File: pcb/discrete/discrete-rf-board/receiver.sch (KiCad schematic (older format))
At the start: 4 parts

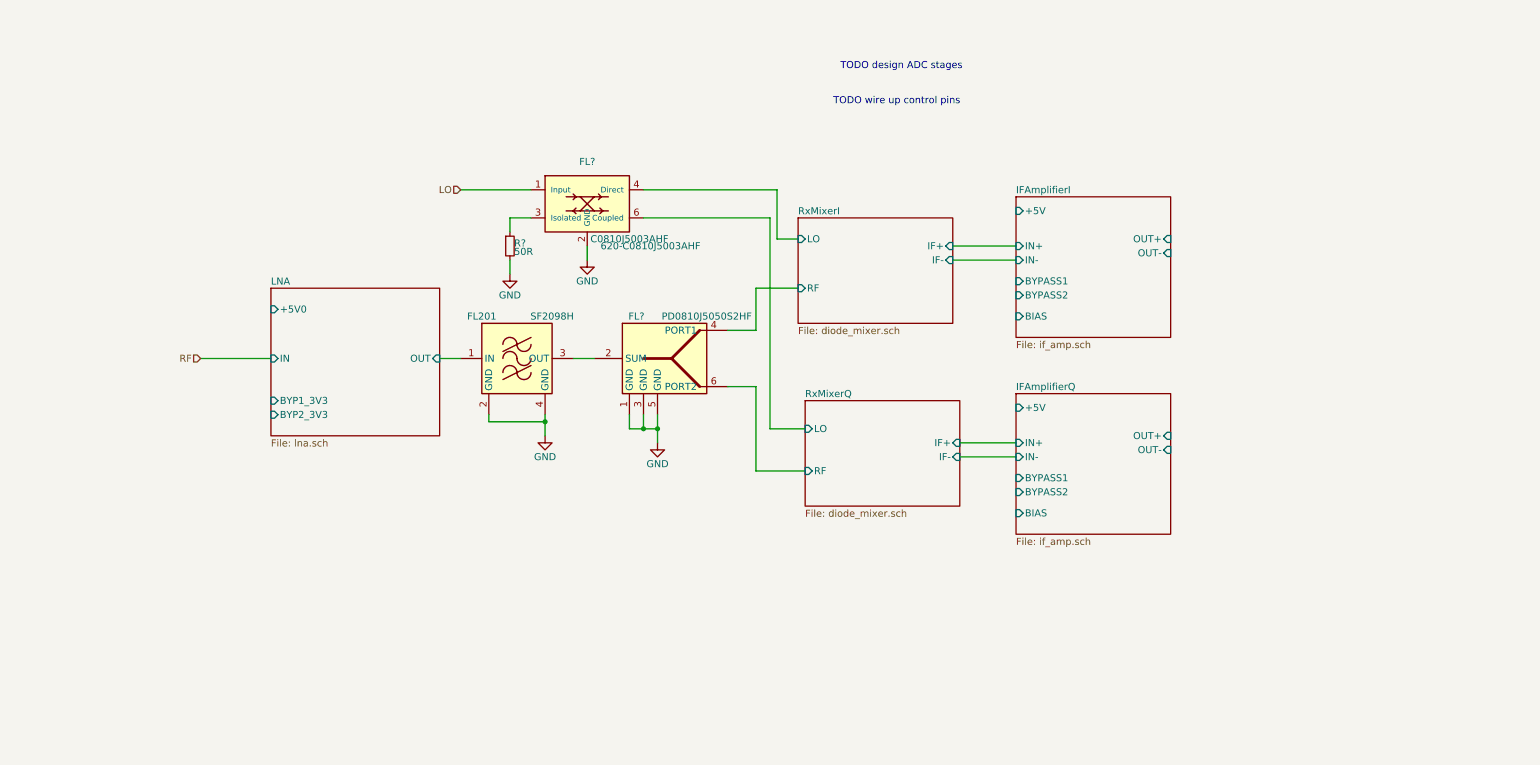
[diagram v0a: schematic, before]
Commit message: Design DAC/ADC stages, pass out all control signals to top sheet
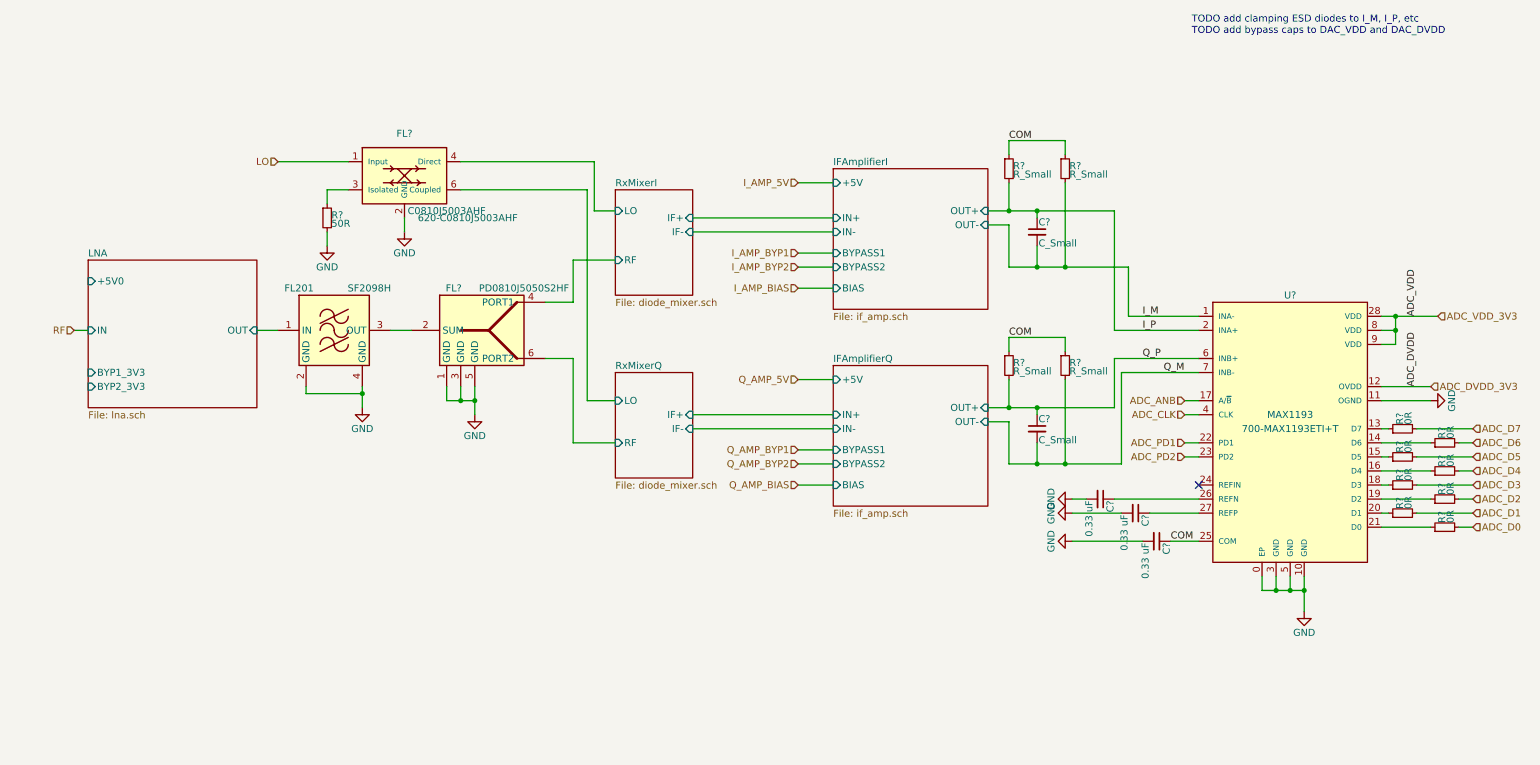
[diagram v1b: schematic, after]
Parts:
- added C? (x2): C_Small, symbol Device:C_Small
- added C? (x3): 0.33 uF, symbol Device:C_Small
- added R? (x4): R_Small, symbol Device:R_Small
- added R? (x8): 0R, symbol Device:R_Small
- added U?: MAX1193, symbol discrete-parts:MAX1193
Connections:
- net GND: now also C?.2, C?.2, C?.2, U?.0 (EP), U?.10 (GND), U?.11 (OGND), U?.3 (GND), U?.5 (GND)
- new net: R?.1, U?.13 (D7)
- new net: R?.1, U?.14 (D6)
- new net: R?.1, U?.15 (D5)
- new net: R?.1, U?.16 (D4)
- new net: R?.1, U?.18 (D3)
- new net: R?.1, U?.19 (D2)
- new net: R?.1, U?.20 (D1)
- new net: R?.1, U?.21 (D0)
- new net: C?.1, U?.26 (REFN)
- new net: C?.1, U?.27 (REFP)
- new net ADC_ANB: U?.17 (A/~B)
- new net ADC_CLK: U?.4 (CLK)
- new net ADC_D0: R?.2
- new net ADC_D1: R?.2
- new net ADC_D2: R?.2
- new net ADC_D3: R?.2
- new net ADC_D4: R?.2
- new net ADC_D5: R?.2
- new net ADC_D6: R?.2
- new net ADC_D7: R?.2
- new net ADC_DVDD_3V3: U?.12 (OVDD)
- new net ADC_PD1: U?.22 (PD1)
- new net ADC_PD2: U?.23 (PD2)
- new net ADC_VDD_3V3: U?.28 (VDD), U?.8 (VDD), U?.9 (VDD)
- new net COM: C?.1, R?.1, R?.1, R?.1, R?.1, U?.25 (COM)
- new net I_M: C?.2, R?.2, U?.1 (INA-)
- new net I_P: C?.1, R?.2, U?.2 (INA+)
- new net Q_M: C?.2, R?.2, U?.7 (INB-)
- new net Q_P: C?.1, R?.2, U?.6 (INB+)
- no-connect marks 0 -> 1
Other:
- note added: "TODO add clamping ESD diodes to I_M, I_P, etc\nTODO add bypass caps to DAC_VDD and DAC_DVDD"
- note removed: "TODO design ADC stages"
- note removed: "TODO wire up control pins"
- moved on the sheet: FL201, FL?, R?

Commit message: Wire out all control signals to connectors TODO PLL charge pump loop, bypass caps in attenuator circuit, antialiasing filter for ADC frontend
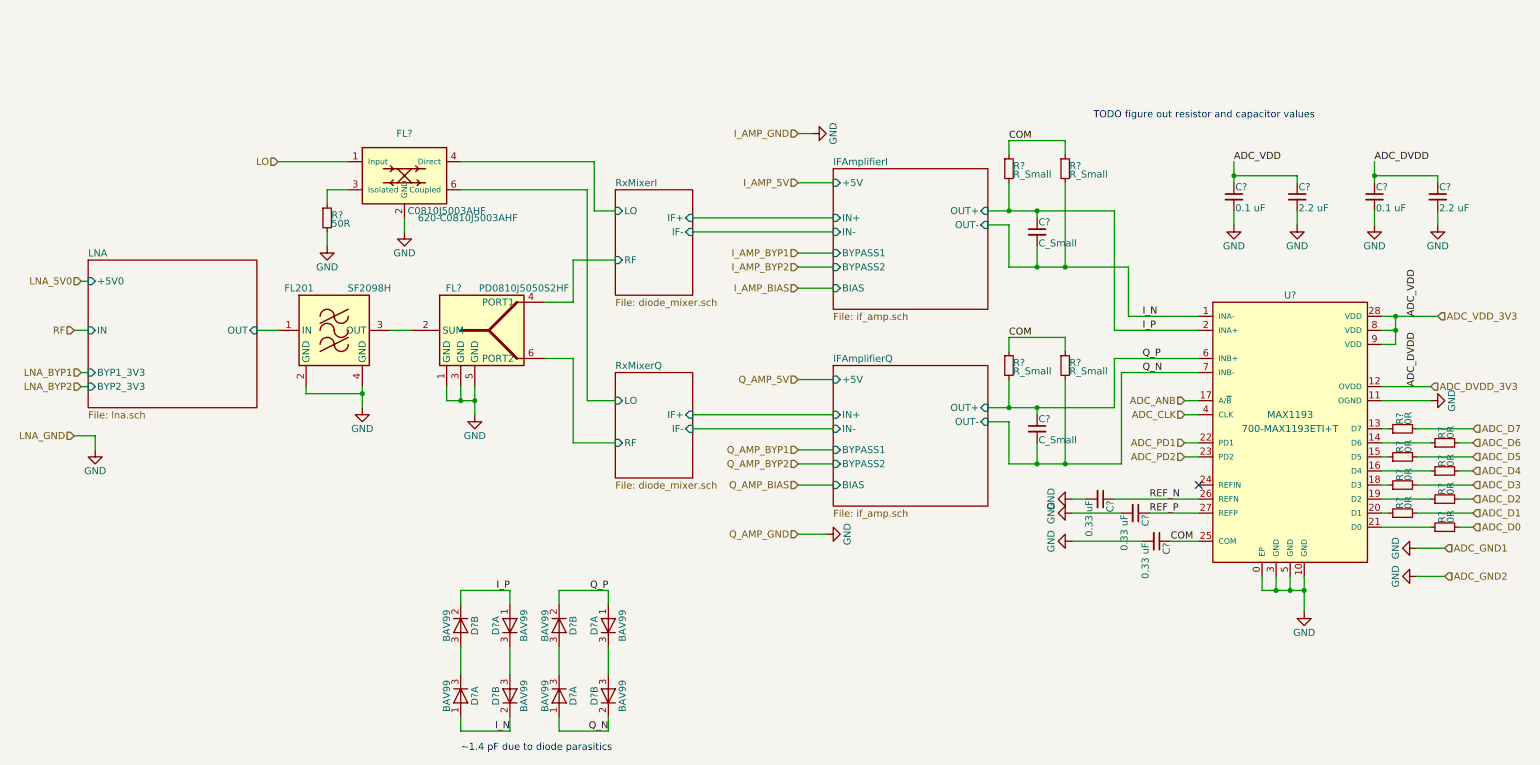
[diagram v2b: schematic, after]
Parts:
- added C? (x2): 2.2 uF, symbol Device:C_Small
- added C? (x2): 0.1 uF, symbol Device:C_Small
- added D? (x8): BAV99, Package_TO_SOT_SMD:SOT-23, symbol Diode:BAV99
- FL201: Mouser (none) -> 719-SF2098H
- FL?: Mouser (none) -> 620-PD0810J5050S2HF
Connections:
- net ADC_DVDD_3V3: now also C?.1, C?.1
- net ADC_VDD_3V3: now also C?.1, C?.1
- net GND: now also C?.2, C?.2, C?.2, C?.2
- net I_P: now also D?.1 (A), D?.2 (K)
- net Q_P: now also D?.1 (A), D?.2 (K)
- net REF_N: now reaches C?.1, U?.26 (REFN)
- net REF_P: now reaches C?.1, U?.27 (REFP)
- net I_M renamed I_N
- net I_N: now also D?.1 (A), D?.2 (K)
- net Q_M renamed Q_N
- net Q_N: now also D?.1 (A), D?.2 (K)
- new net: D?.3 (A), D?.3 (K) (x4)
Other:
- note added: "TODO figure out resistor and capacitor values"
- note added: "~~1.4 pF due to diode parasitics"
- note removed: "TODO add clamping ESD diodes to I_M, I_P, etc\nTODO add bypass caps to DAC_VDD and DAC_DVDD"

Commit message: The footprintening continues
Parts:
- added R?: 51R 0603, symbol Device:R_Small
- FL?: footprint (none) -> discrete_footprints:Anaren_PD0810J5050S2HF
- FL?: footprint (none) -> discrete_footprints:Anaren_C0810J5003AHF
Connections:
- net RxMixerI/RF: now also R?.1
- net RxMixerQ/RF: now also R?.2
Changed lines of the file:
@@
 	900  3600 1000 3600
 Wire Wire Line
-	4250 3400 4450 3400
+	4250 3400 4350 3400
 Wire Wire Line
 	4450 3400 4450 3100
@@
 	4450 3100 4750 3100
 Wire Wire Line
-	4250 3800 4450 3800
+	4250 3800 4350 3800
 Wire Wire Line
 	4450 3800 4450 4400
@@
 F 0 "FL?" H 3600 3900 50  0000 C CNN
 F 1 "PD0810J5050S2HF" H 4100 3900 50  0000 C CNN
-F 2 "" H 3750 3150 50  0001 C CNN
+F 2 "discrete_footprints:Anaren_PD0810J5050S2HF" H 3750 3150 50  0001 C CNN
 F 3 "" H 4150 3050 50  0001 C CNN
 F 4 " 620-PD0810J5050S2HF" H 3850 3600 50  0001 C CNN "Mouser"
@@
 F 0 "FL?" H 3250 2200 50  0000 C CNN
 F 1 "C0810J5003AHF" H 3550 1650 50  0000 C CNN
-F 2 "" H 3250 2200 50  0001 C CNN
+F 2 "discrete_footprints:Anaren_C0810J5003AHF" H 3250 2200 50  0001 C CNN
 F 3 "" H 3250 2200 50  0001 C CNN
 F 4 " 620-C0810J5003AHF " H 3700 1600 50  0000 C CNN "Mouser"
@@
 Wire Wire Line
 	10450 5350 10650 5350
+$Comp
+L Device:R_Small R?
+U 1 1 5DC881F5
+P 4350 3600
+F 0 "R?" H 4380 3620 50  0000 L CNN
+F 1 "51R 0603" H 4380 3560 50  0000 L CNN
+F 2 "" H 4350 3600 50  0001 C CNN
+F 3 "~" H 4350 3600 50  0001 C CNN
+	1    4350 3600
+	1    0    0    -1
+$EndComp
+Wire Wire Line
+	4350 3700 4350 3800
+Connection ~ 4350 3800
+Wire Wire Line
+	4350 3800 4450 3800
+Wire Wire Line
+	4350 3500 4350 3400
+Connection ~ 4350 3400
+Wire Wire Line
+	4350 3400 4450 3400
 $EndSCHEMATC

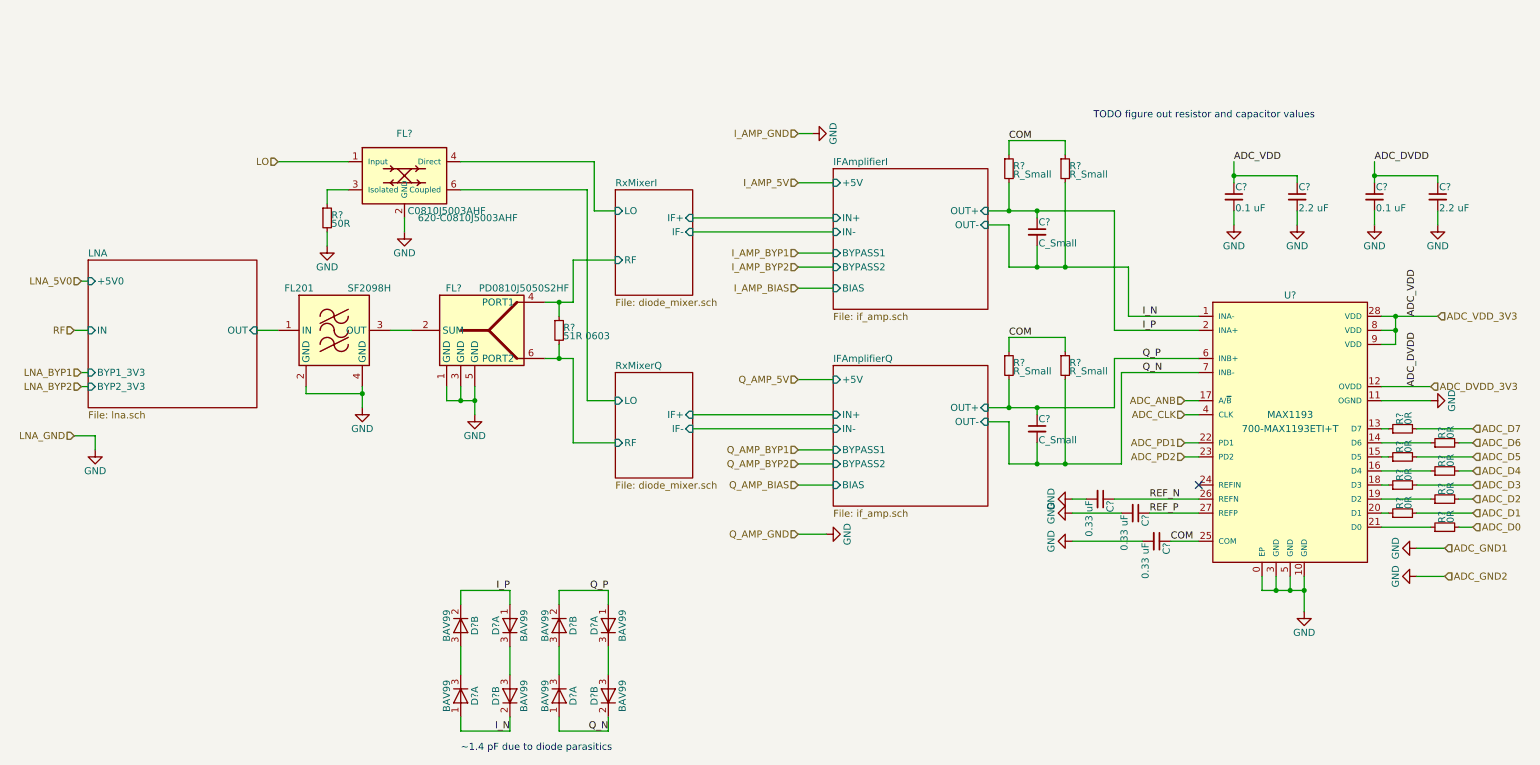
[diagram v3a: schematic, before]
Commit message: Add matching PNP/NPN transistor pairs, fix pin numbering for BFU520R transistors TODO fix biasing on power stage, source last NPN transistor, autofill and start sourcing passives
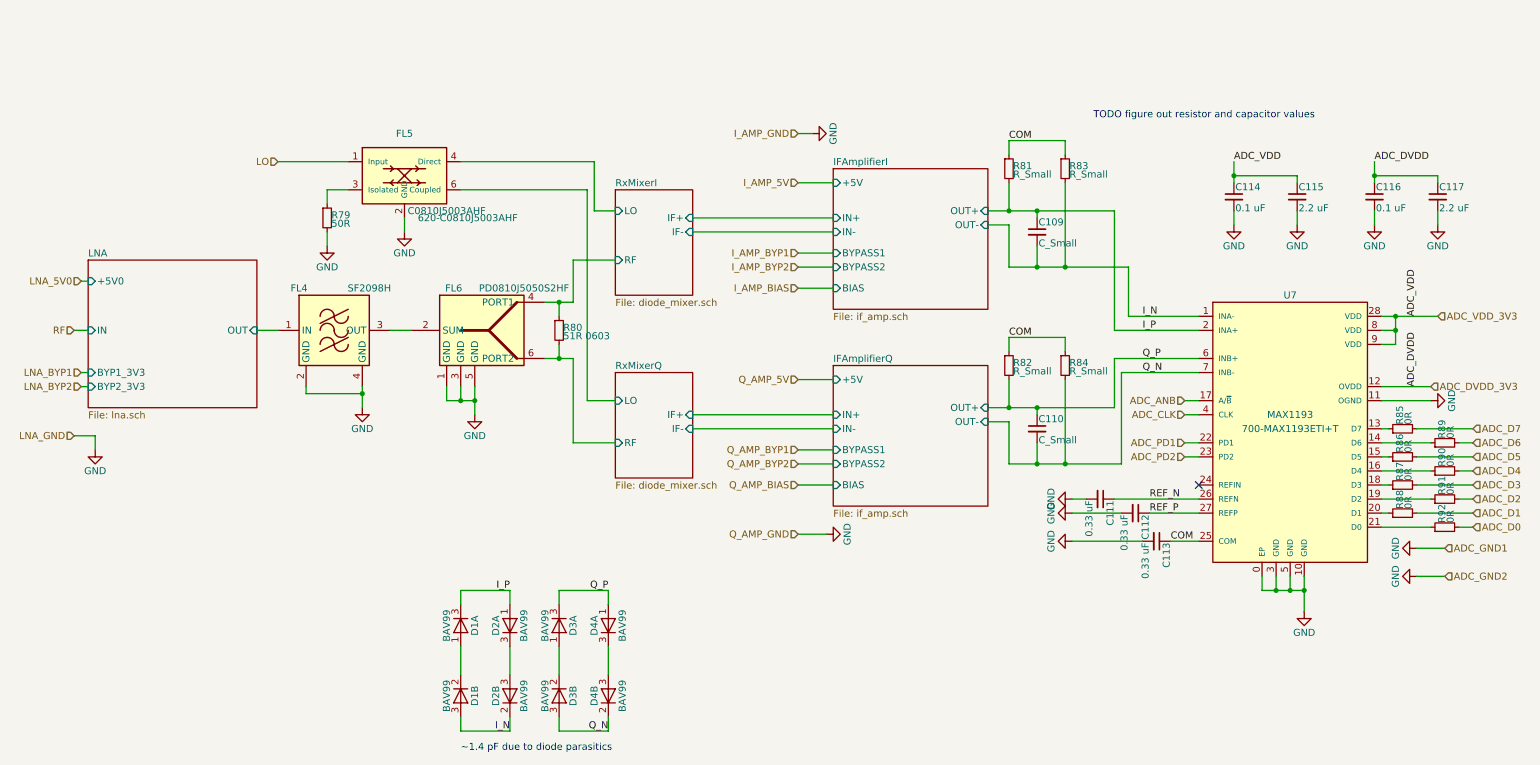
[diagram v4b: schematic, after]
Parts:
- gave numbers to parts that had none: 30
- renumbered FL201 to FL4
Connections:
- net I_N: now also D1.3 (A); no longer D1.1 (A)
- net I_P: now also D1.3 (K); no longer D1.2 (K)
- net Q_N: now also D3.3 (A); no longer D3.1 (A)
- net Q_P: now also D3.3 (K); no longer D3.2 (K)
- new net: D1.1 (A), D1.2 (K)
- new net: D3.1 (A), D3.2 (K)
